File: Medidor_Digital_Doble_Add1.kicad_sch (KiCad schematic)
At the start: 12 parts, among them J1 Screw_Terminal_01x01, J2 Screw_Terminal_01x01, J3 Screw_Terminal_01x01, J4 Screw_Terminal_01x01, J5 Screw_Terminal_01x01, J6 Screw_Terminal_01x01, U1 INA823

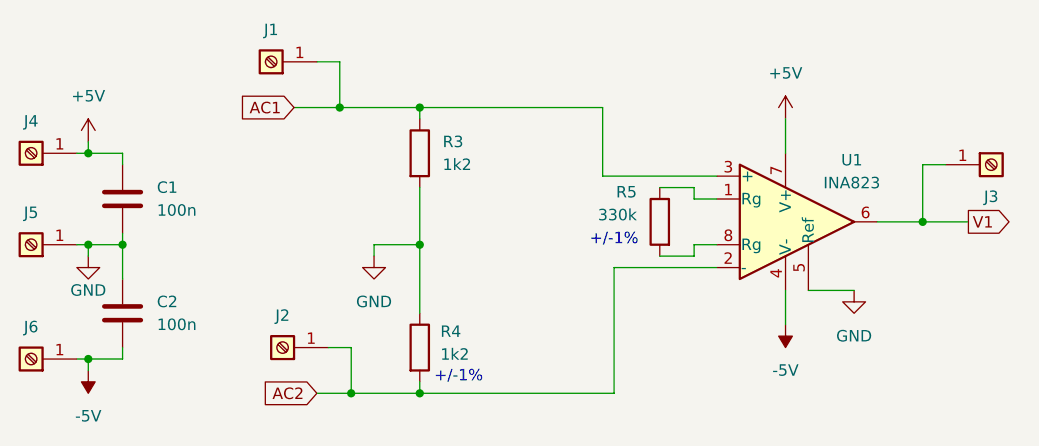
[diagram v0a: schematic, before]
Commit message: SCH:Se cambia la resistencia de 1.2k a 1k. PCB:Se rediseña la distribución para menor altura de la placa.
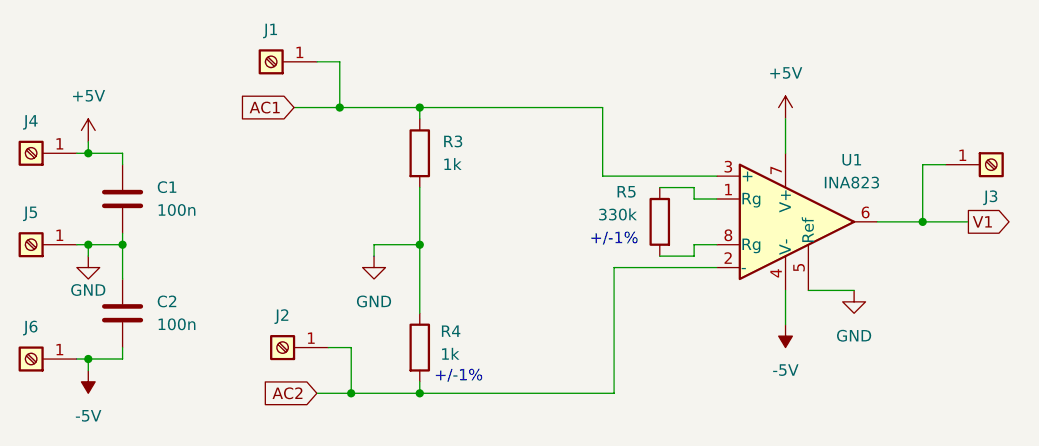
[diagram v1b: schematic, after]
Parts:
- R3, R4: value 1k2 -> 1k
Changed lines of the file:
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@@
 			)
 		)
-		(property "Value" "1k2"
+		(property "Value" "1k"
 			(at 116.84 62.23 0)
 			(effects
@@
 			)
 		)
-		(property "Value" "1k2"
+		(property "Value" "1k"
 			(at 116.586 83.312 0)
 			(effects
